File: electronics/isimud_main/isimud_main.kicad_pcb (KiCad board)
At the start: 2 copper layers, 1 part

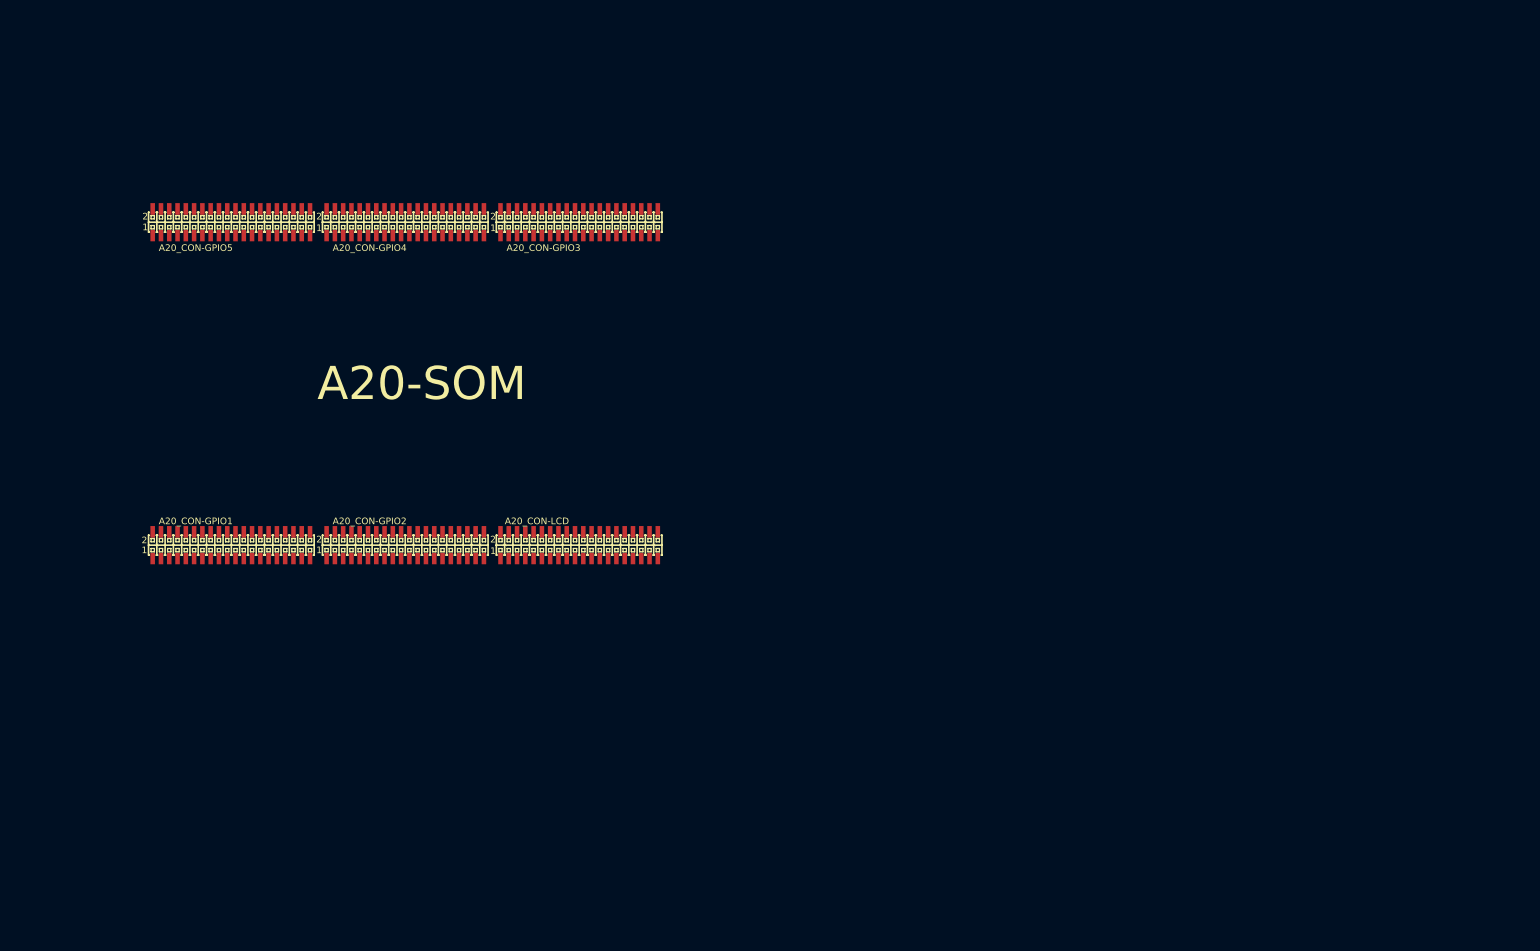
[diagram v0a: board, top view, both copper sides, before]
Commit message: parts placed on print board
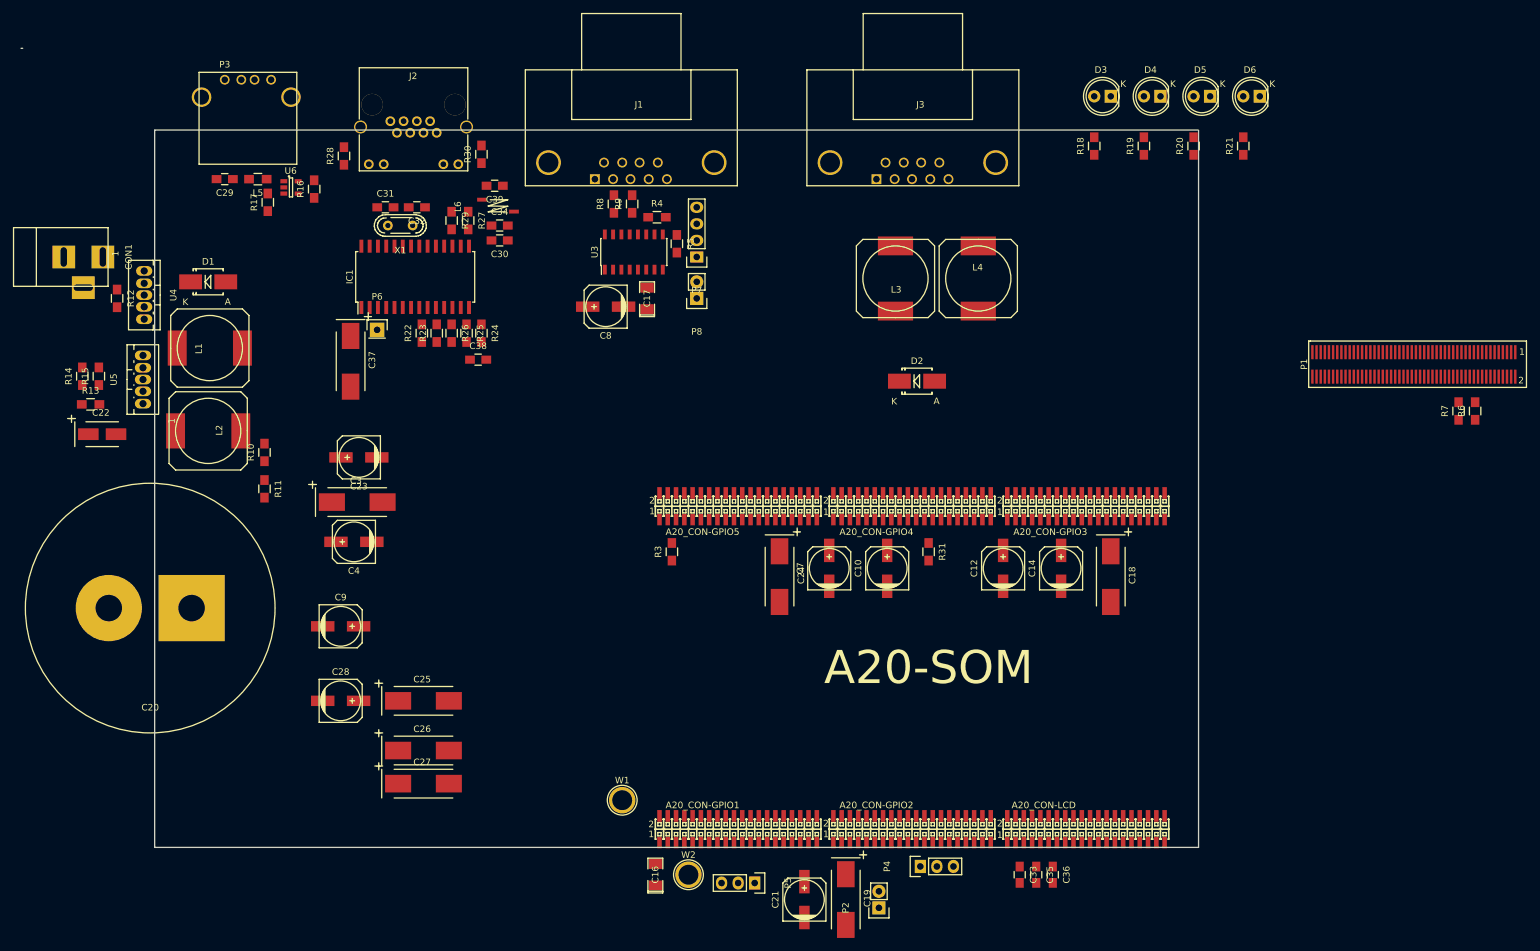
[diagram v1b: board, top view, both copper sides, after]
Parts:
- removed ?: , KiCAD connector library:A20-SOM
- added C10: 47uF 16V, Capacitors_SMD:c_elec_6.3x5.8, F.Cu at (212.3, 117.2)
- added C12: 47uF 16V, Capacitors_SMD:c_elec_6.3x5.8, F.Cu at (230.1, 117.2)
- added C14: 47uF 16V, Capacitors_SMD:c_elec_6.3x5.8, F.Cu at (239.0, 117.2)
- added C16: 1uF, SMD_Packages:SMD-1206_Pol, F.Cu at (176.8, 164.2)
- added C17: 1uF, SMD_Packages:SMD-1206_Pol, F.Cu at (175.5, 75.8)
- added C18: 10uF, Capacitors_Tantalum_SMD:TantalC_SizeD_EIA-7343_HandSoldering, F.Cu at (246.6, 118.5)
- added C19: 22uF 6.3v, Capacitors_Tantalum_SMD:TantalC_SizeD_EIA-7343_HandSoldering, F.Cu at (206.0, 168.0)
- added C20: 1000uF 16V, Discret:CP36V, F.Cu at (99.3, 123.3)
- added C21: 220uF 16V, Capacitors_SMD:c_elec_6.3x5.8, F.Cu at (199.6, 168.0)
- added C22: 1000uF 16V, Capacitors_Tantalum_SMD:TantalC_SizeB_EIA-3528_HandSoldering, F.Cu at (91.9, 96.6)
- added C23: 220uF 16V, Capacitors_SMD:c_elec_6.3x5.8, F.Cu at (131.3, 100.2)
- added C24: 22uF/6.3V, Capacitors_Tantalum_SMD:TantalC_SizeD_EIA-7343_HandSoldering, F.Cu at (195.8, 118.5)
- added C25: 22uF/6.3V, Capacitors_Tantalum_SMD:TantalC_SizeD_EIA-7343_HandSoldering, F.Cu at (141.2, 137.5)
- added C26: 22uF/6.3V, Capacitors_Tantalum_SMD:TantalC_SizeD_EIA-7343_HandSoldering, F.Cu at (141.2, 145.2)
- added C27: 100uF/16V/LOWESR/105C/6.3x11mm_RM2.5, Capacitors_Tantalum_SMD:TantalC_SizeD_EIA-7343_HandSoldering, F.Cu at (141.2, 150.2)
- added C28: 220uF/10V/tant, Capacitors_SMD:c_elec_6.3x5.8, F.Cu at (128.5, 137.5)
- added C29: 100nF, Capacitors_SMD:C_0805_HandSoldering, F.Cu at (110.7, 57.5)
- added C3: 33uF 16V, Capacitors_Tantalum_SMD:TantalC_SizeD_EIA-7343_HandSoldering, F.Cu at (131.1, 107.1)
- added C30: 100nF, Capacitors_SMD:C_0805_HandSoldering, F.Cu at (152.9, 66.9)
- added C31: 18pF, Capacitors_SMD:C_0805_HandSoldering, F.Cu at (135.4, 61.8)
- added C32: 18pF, Capacitors_SMD:C_0805_HandSoldering, F.Cu at (140.2, 61.8)
- added C33: 100nF, Capacitors_SMD:C_0805_HandSoldering, F.Cu at (232.7, 164.2)
- added C34: 100nF, Capacitors_SMD:C_0805_HandSoldering, F.Cu at (152.9, 64.6)
- added C35: 100nF, Capacitors_SMD:C_0805_HandSoldering, F.Cu at (235.2, 164.2)
- added C36: 100nF, Capacitors_SMD:C_0805_HandSoldering, F.Cu at (237.7, 164.2)
- added C37: 10uF, Capacitors_Tantalum_SMD:TantalC_SizeD_EIA-7343_HandSoldering, F.Cu at (130.0, 85.5)
- added C38: 10nF, Capacitors_SMD:C_0805_HandSoldering, F.Cu at (149.6, 85.2)
- added C39: 100nF, Capacitors_SMD:C_0805_HandSoldering, F.Cu at (152.1, 58.5)
- added C4: 1uF 16V, Capacitors_SMD:c_elec_6.3x5.8, F.Cu at (130.6, 113.2)
- added C7: 47uF 16V, Capacitors_SMD:c_elec_6.3x5.8, F.Cu at (203.5, 117.2)
- added C8: 1uF, Capacitors_SMD:c_elec_6.3x5.8, F.Cu at (169.2, 77.1)
- added C9: 1uF, Capacitors_SMD:c_elec_6.3x5.8, F.Cu at (128.5, 126.1)
- added CON1: 12V DC, Connect:BARREL_JACK, F.Cu at (85.9, 69.5)
- added D1: 1N5822, Diodes_SMD:SMB_Handsoldering, F.Cu at (108.2, 73.3)
- added D2: 1N5822, Diodes_SMD:SMB_Handsoldering, F.Cu at (216.9, 88.5)
- added D3: SAT_ON, LEDs:LED-5MM, F.Cu at (246.6, 44.8)
- added D4: GPS_ON, LEDs:LED-5MM, F.Cu at (254.3, 44.8)
- added D5: PWR_ON, LEDs:LED-5MM, F.Cu at (261.9, 44.8)
- added D6: STATUS, LEDs:LED-5MM, F.Cu at (269.5, 44.8)
- added IC1: ENC28J60-I/SO, Housings_SOIC:SOIC-28_7.5x17.9mm_Pitch1.27mm, F.Cu at (140.0, 72.5)
- added J1: DB9, Connect:DB9FC, F.Cu at (173.0, 56.3)
- added J2: RJ45-TRANSFO, Connect:RJHSE538X, F.Cu at (136.1, 48.6)
- added J3: DB9, Connect:DB9FC, F.Cu at (216.2, 56.3)
- added L1: 100uH, Inductors:SELF-WE-PD-XXL, F.Cu at (108.5, 83.4)
- added L2: 100uH, Inductors:SELF-WE-PD-XXL, F.Cu at (108.2, 96.1)
- added L3: 100uH, Inductors:SELF-WE-PD-XXL, F.Cu at (213.6, 72.8)
- added L4: 100uH, Inductors:SELF-WE-PD-XXL, F.Cu at (226.3, 72.8)
- added L5: FB0805/600R/2A, Resistors_SMD:R_0805_HandSoldering, F.Cu at (115.8, 57.5)
- added L6: ferrite bead, Air_Coils_SML_NEOSID:Neosid_Air-Coil_SML_2turn_HAM0231A, F.Cu at (152.7, 61.6)
- added P1: CONN_02X50, KiCAD connector library:BB-2X50-SMD, F.Cu at (308.9, 86.7)
- added P2: LIPO_BAT, Socket_Strips:Socket_Strip_Straight_1x02, F.Cu at (211.1, 169.3)
- added P3: USB_A, Connect:USB_A, F.Cu at (110.7, 42.3)
- added P4: UART_0, Pin_Headers:Pin_Header_Straight_1x03, F.Cu at (217.4, 162.9)
- added P5: UART_4, Pin_Headers:Pin_Header_Straight_1x03, F.Cu at (192.0, 165.5)
- added P6: ETH_CLKOUT, Pin_Headers:Pin_Header_Straight_1x01, F.Cu at (134.1, 80.6)
- added P7: RS232-UART, Pin_Headers:Pin_Header_Straight_1x04, F.Cu at (183.1, 69.5)
- added P8: RS232-2, Pin_Headers:Pin_Header_Straight_1x02, F.Cu at (183.1, 75.8)
- added R10: 2k, Resistors_SMD:R_0805_HandSoldering, F.Cu at (116.8, 99.4)
- added R11: 1k, Resistors_SMD:R_0805_HandSoldering, F.Cu at (116.8, 105.0)
- added R12: 1k, Resistors_SMD:R_0805_HandSoldering, F.Cu at (94.2, 75.8)
- added R13: 1k2, Resistors_SMD:R_0805_HandSoldering, F.Cu at (90.2, 92.1)
- added R14: 1k2, Resistors_SMD:R_0805_HandSoldering, F.Cu at (88.9, 87.8)
- added R15: 1k, Resistors_SMD:R_0805_HandSoldering, F.Cu at (91.4, 87.8)
- added R16: 10k, Resistors_SMD:R_0805_HandSoldering, F.Cu at (124.5, 59.1)
- added R17: 13k %1, Resistors_SMD:R_0805_HandSoldering, F.Cu at (117.3, 61.1)
- added R18: 220R, Resistors_SMD:R_0805_HandSoldering, F.Cu at (244.1, 52.5)
- added R19: 220R, Resistors_SMD:R_0805_HandSoldering, F.Cu at (251.7, 52.5)
- added R20: 220R, Resistors_SMD:R_0805_HandSoldering, F.Cu at (259.3, 52.5)
- added R21: 220R, Resistors_SMD:R_0805_HandSoldering, F.Cu at (267.0, 52.5)
- added R22: 100k, Resistors_SMD:R_0805_HandSoldering, F.Cu at (141.0, 81.2)
- added R23: 10k, Resistors_SMD:R_0805_HandSoldering, F.Cu at (143.3, 81.2)
- added R24: 2k2 %1, Resistors_SMD:R_0805_HandSoldering, F.Cu at (150.1, 81.2)
- added R25: 49.9 %1, Resistors_SMD:R_0805_HandSoldering, F.Cu at (147.8, 81.2)
- added R26: 49.9 %1, Resistors_SMD:R_0805_HandSoldering, F.Cu at (145.5, 81.2)
- added R27: 49.9 %1, Resistors_SMD:R_0805_HandSoldering, F.Cu at (148.1, 63.9)
- added R28: 180R, Resistors_SMD:R_0805_HandSoldering, F.Cu at (129.0, 54.0)
- added R29: 49.9 %1, Resistors_SMD:R_0805_HandSoldering, F.Cu at (145.5, 63.9)
- added R3: 10k, Resistors_SMD:R_0805_HandSoldering, F.Cu at (179.3, 114.7)
- added R30: 180R, Resistors_SMD:R_0805_HandSoldering, F.Cu at (150.1, 53.7)
- added R31: 0R, Resistors_SMD:R_0805_HandSoldering, F.Cu at (218.7, 114.7)
- added R4: 2k2, Resistors_SMD:R_0805_HandSoldering, F.Cu at (177.0, 63.4)
- added R5: 2k2, Resistors_SMD:R_0805_HandSoldering, F.Cu at (180.1, 67.4)
- added R6: 330, Resistors_SMD:R_0805_HandSoldering, F.Cu at (302.5, 93.1)
- added R7: 330, Resistors_SMD:R_0805_HandSoldering, F.Cu at (300.0, 93.1)
- added R8: 0R, Resistors_SMD:R_0805_HandSoldering, F.Cu at (170.4, 61.3)
- added R9: 0R, Resistors_SMD:R_0805_HandSoldering, F.Cu at (173.2, 61.3)
- added U1: SOM-A20, KiCAD connector library:A20-SOM, F.Cu at (216.2, 132.5)
- added U3: MAX232, Housings_SOIC:SOIC-16_3.9x9.9mm_Pitch1.27mm, F.Cu at (173.5, 68.7)
- added U4: LM2576, TO_SOT_Packages_THT:Pentawatt_Neutral_Straight_Vertical_TO220-5-T05A, F.Cu at (97.8, 75.3)
- added U5: LM2576, TO_SOT_Packages_THT:Pentawatt_Neutral_Straight_Vertical_TO220-5-T05A, F.Cu at (98.8, 88.3)
- added U6: SY6280, TO_SOT_Packages_SMD:SOT-23-5, F.Cu at (120.9, 58.8)
- added W1: GNDA, Connect:1pin, F.Cu at (171.7, 152.8)
- added W2: 5V OTG, Connect:1pin, F.Cu at (181.9, 164.2)
- added X1: CRYSTAL_SMD, Crystals:Crystal_HC52-U_Vertical, F.Cu at (137.7, 64.6)
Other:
- board outline added: 180.6 x 122.6 mm

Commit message: pcb design is done,last checks for gerber
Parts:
- removed C24, C25, C26: 22uF/6.3V, Capacitors_Tantalum_SMD:TantalC_SizeD_EIA-7343_HandSoldering
- removed C27: 100uF/16V/LOWESR/105C/6.3x11mm_RM2.5, Capacitors_Tantalum_SMD:TantalC_SizeD_EIA-7343_HandSoldering
- removed C28: 220uF/10V/tant, Capacitors_SMD:c_elec_6.3x5.8
- removed C29: 100nF, Capacitors_SMD:C_0805_HandSoldering
- removed R16: 10k, Resistors_SMD:R_0805_HandSoldering
- removed R17: 13k %1, Resistors_SMD:R_0805_HandSoldering
- removed U6: SY6280, TO_SOT_Packages_SMD:SOT-23-5
- added C1: 33pF, Capacitors_SMD:C_0805_HandSoldering, F.Cu at (134.0, 115.8)
- added C11: 47uF 16V, Capacitors_SMD:c_elec_6.3x5.8, F.Cu at (82.9, 133.6)
- added C13: 100nF, Capacitors_SMD:C_0805_HandSoldering, F.Cu at (90.7, 114.0)
- added C2: 33pF, Capacitors_SMD:C_0805_HandSoldering, F.Cu at (134.0, 118.4)
- added C5: 33pF, Capacitors_SMD:C_0805_HandSoldering, F.Cu at (94.6, 117.5)
- added C6: 100nF, Capacitors_SMD:C_0805_HandSoldering, F.Cu at (89.4, 103.9)
- added P9: AKTIF GPS ANTEN, Connect:bnc-ci, F.Cu at (78.7, 105.6)
- added R1: 0R, Resistors_SMD:R_0805_HandSoldering, F.Cu at (85.7, 140.3)
- added R2: 0R, Resistors_SMD:R_0805_HandSoldering, F.Cu at (90.7, 121.0)
- added U2: SIMCARD_HOLDER, KiCAD connector library:SIMCARD, F.Cu at (114.8, 116.1)
- C20: footprint Discret:CP36V -> Capacitors_ThroughHole:C_Radial_D10_L13_P5
- J2: footprint Connect:RJHSE538X -> KiCAD connector library:RJHSE538X
- L5: value FB0805/600R/2A -> 100uH; footprint Resistors_SMD:R_0805_HandSoldering -> Inductors:SELF-WE-PD-XXL
- P1, R29: moved to B.Cu
- P3: value USB_A -> SAT MODULE GPS; footprint Connect:USB_A -> Connect:bnc-ci
- moved R6 207.3 mm to (97.5, 124.1), turned to 270 degrees
- moved D5 201.7 mm to (60.2, 48.8), turned to 90 degrees
- moved R7 199.0 mm to (103.8, 126.9), turned to 180 degrees
- moved R20 194.4 mm to (65.0, 47.5)
- moved P1 190.1 mm to (124.3, 132.3)
- moved C14 174.0 mm to (65.0, 121.3), turned to 180 degrees
- moved D6 171.5 mm to (98.2, 36.8)
- moved R21 170.4 mm to (96.9, 41.8), turned to 180 degrees
- moved D3 167.5 mm to (79.4, 36.7)
- moved R18 166.5 mm to (78.0, 41.5), turned to 180 degrees
- moved C12 166.3 mm to (65.0, 97.2), turned to 180 degrees
- moved D4 165.7 mm to (88.8, 36.7)
- moved R19 164.8 mm to (87.2, 41.5), turned to 180 degrees
- moved C10 147.4 mm to (65.0, 113.3), turned to 180 degrees
- moved L4 147.0 mm to (79.6, 82.8)
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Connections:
- C21 pad 1: +5VP -> PWR_LED
- L2 pad 2: +5VP -> PWR_LED
- L5 pad 2: Net-(C29-Pad1) -> Net-(C13-Pad2)
- P3 pad 1: Net-(C29-Pad1) -> Net-(C13-Pad1)
- P3 pad 2: UDM1 -> Net-(C11-Pad2)
- U1 pad 2-1: +5VP -> PWR_LED
- U1 pad 5-11: STATUS_LED -> PG5
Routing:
- net GND: track 0.00 -> 958.3 mm, vias 0 -> 14
- net +5V: track 0.00 -> 480.1 mm, vias 0 -> 6
- net +3V3: track 0.00 -> 303.6 mm, vias 0 -> 7
- net PWR_LED: track 0.00 -> 215.6 mm, vias 0 -> 3
- net +6V: track 0.00 -> 195.8 mm, vias 0 -> 4
- net UART7_RX: track 0.00 -> 150.4 mm, vias 0 -> 2
- net TWI1_SDA: track 0.00 -> 133.6 mm, vias 0 -> 2
- net SAT_LED: track 0.00 -> 127.1 mm, vias 0 -> 2
- net GPS_LED: track 0.00 -> 121.4 mm, vias 0 -> 2
- net TWI1_SCK: track 0.00 -> 120.6 mm, vias 0 -> 2
- net UART3_RX: track 0.00 -> 100.5 mm, vias 0 -> 1
- net PG8: track 0.00 -> 94.6 mm, vias 0 -> 1
- net PG10: track 0.00 -> 89.8 mm, vias 0 -> 1
- net PG9: track 0.00 -> 88.5 mm, vias 0 -> 1
- net PG6: track 0.00 -> 87.5 mm, vias 0 -> 1
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- added copper zone on B.Cu, net GND
- added copper zone on F.Cu, net GND
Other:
- board size 180.6 x 122.6 mm -> 160.3 x 110.1 mm
- net class Default: trace_width 0.25 -> 0.4; via_dia 0.6 -> 1.2; via_drill 0.4 -> 0.8
- net class POWER added: clearance 0.2, trace_width 0.4, via_dia 1.2, via_drill 0.8
- rule trace_min: 0.2 -> 0.3
- rule via_min_drill: 0.3 -> 0.6
- rule via_min_size: 0.4 -> 1.2
- board text added: "+ -"
- board text added: "4.2V BAT INPUT"
- board text added: "RX TX"
- board text added: "TX RX GND"
- board text added: "TX1 RX1 TX2 RX2"
- board text added: "Teknomobil 2016"

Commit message: new revision for production
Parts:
- moved R7 5.37 mm to (109.2, 126.6)
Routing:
- net Net-(C1-Pad1): track 53.8 -> 31.8 mm, vias 3 -> 1
- net Net-(P1-Pad64): track 37.4 -> 26.0 mm, vias 3 -> 1
- net +5V: track 480.1 -> 469.8 mm
- net GND: track 958.3 -> 948.5 mm
- net +6V: track 195.8 -> 202.7 mm, vias 4 -> 5
- net Net-(C2-Pad1): track 47.6 -> 41.2 mm, vias 2 -> 3
- net UART6_TX: track 70.3 -> 64.9 mm
- net /THURAYA_TX: track 6.57 -> 11.2 mm
- net SAT_ON: track 39.7 -> 35.1 mm
- net Net-(C5-Pad1): track 32.3 -> 28.7 mm
- net SAT_RST: track 53.4 -> 50.9 mm
- net /THURAYA_RX: track 5.16 -> 6.16 mm
- net SAT_OFF: track 41.6 -> 40.8 mm
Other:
- net class POWER: trace_width 0.4 -> 0.5
- rule trace_min: 0.3 -> 0.2
